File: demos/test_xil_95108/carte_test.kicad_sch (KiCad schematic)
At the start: 44 parts

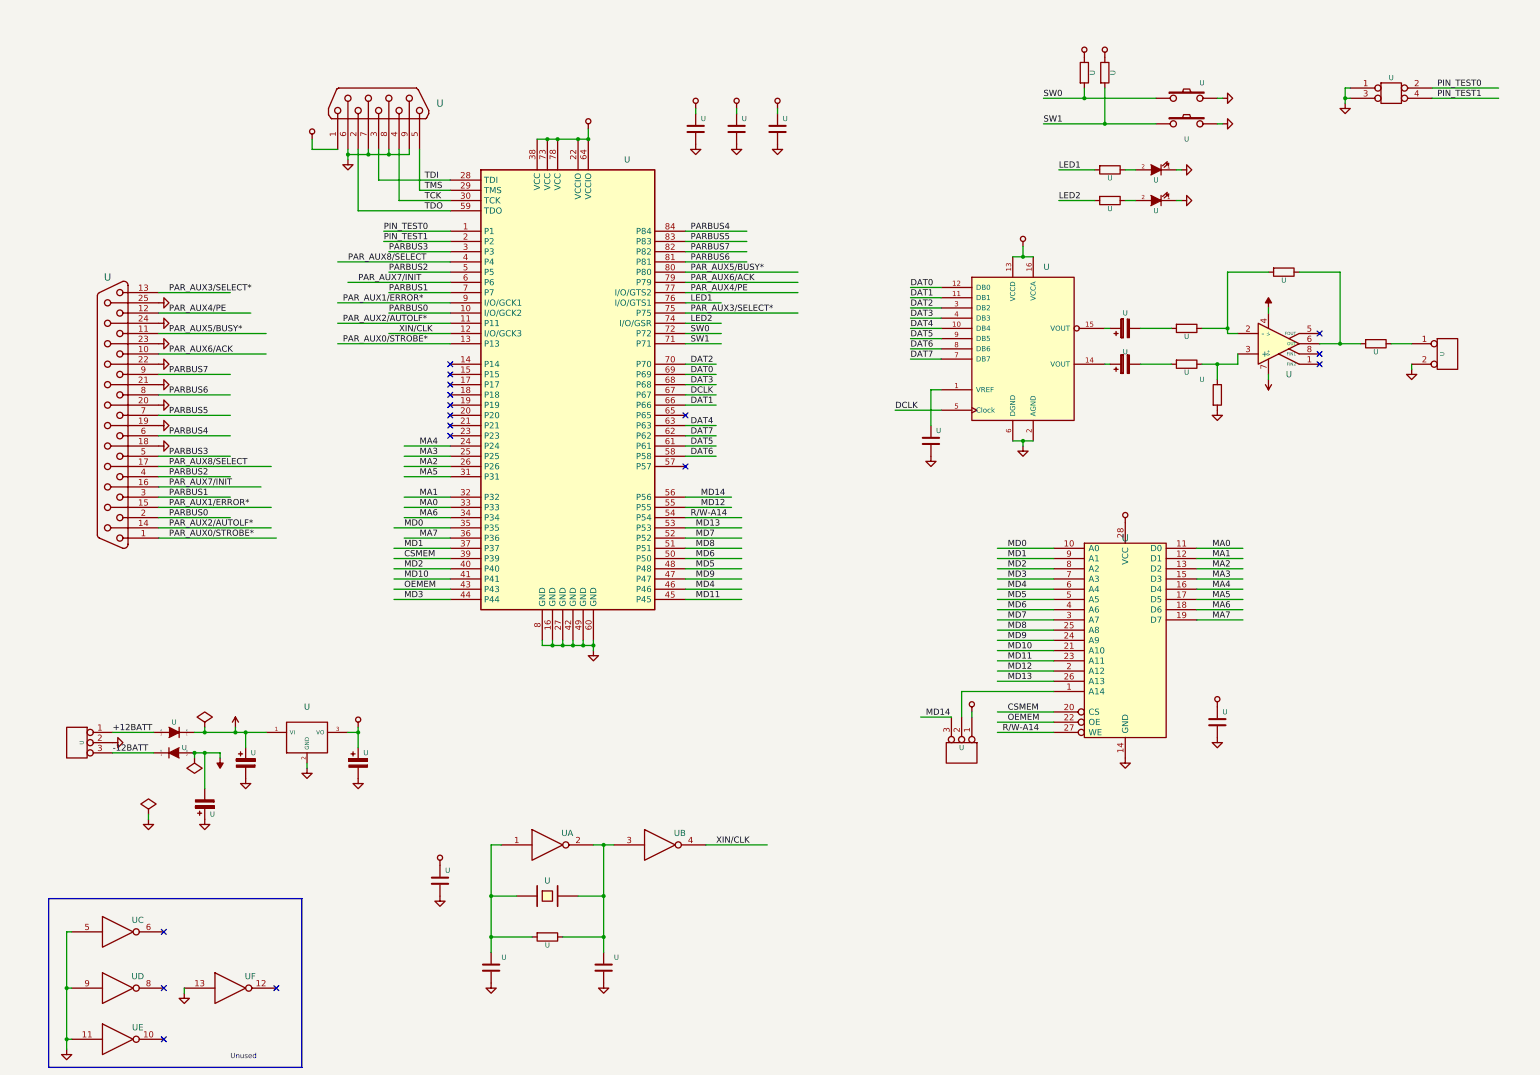
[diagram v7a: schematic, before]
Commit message: Update demos using latest file formats.
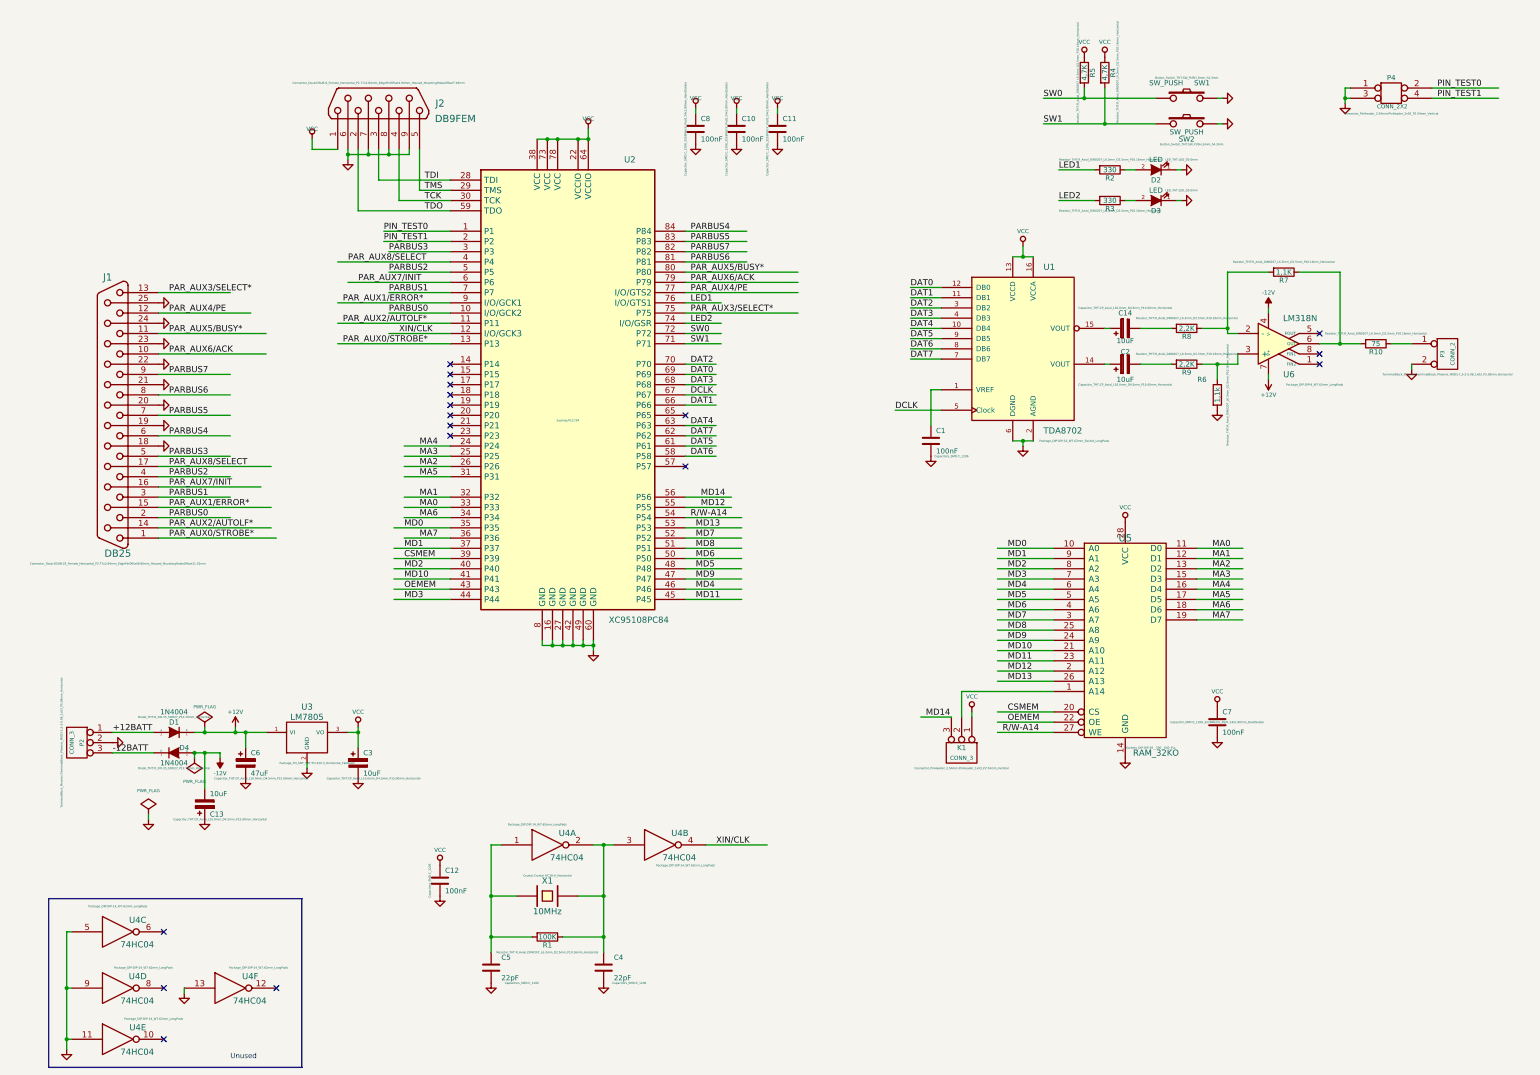
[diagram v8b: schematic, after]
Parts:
- removed U (x2): (no value), symbol carte_test_schlib:-12V
- C1, C12: renamed from U; value (none) -> 100nF; footprint (none) -> Capacitors_SMD:C_1206
- C10, C11, C7, C8: renamed from U; value (none) -> 100nF; footprint (none) -> Capacitor_SMD:C_1206_3216Metric_Pad1.24x1.80mm_HandSolder
- C13, C14, C2, C3: renamed from U; value (none) -> 10uF; footprint (none) -> Capacitor_THT:CP_Axial_L10.0mm_D4.5mm_P15.00mm_Horizontal
- C4, C5: renamed from U; value (none) -> 22pF; footprint (none) -> Capacitors_SMD:C_1206
- C6: renamed from U; value (none) -> 47uF; footprint (none) -> Capacitor_THT:CP_Axial_L10.0mm_D4.5mm_P15.00mm_Horizontal
- D1, D4: renamed from U; value (none) -> 1N4004; footprint (none) -> Diode_THT:D_DO-35_SOD27_P12.70mm_Horizontal
- D2, D3: renamed from U; value (none) -> LED; footprint (none) -> LED_THT:LED_D5.0mm
- J1: renamed from U; value (none) -> DB25; footprint (none) -> Connector_Dsub:DSUB-25_Female_Horizontal_P2.77x2.84mm_EdgePinOffset9.90mm_Housed_MountingHolesOffset11.32mm
- J2: renamed from U; value (none) -> DB9FEM; footprint (none) -> Connector_Dsub:DSUB-9_Female_Horizontal_P2.77x2.84mm_EdgePinOffset4.94mm_Housed_MountingHolesOffset7.48mm
- K1: renamed from U; value (none) -> CONN_3; footprint (none) -> Connector_PinHeader_2.54mm:PinHeader_1x03_P2.54mm_Vertical
- P2: renamed from U; value (none) -> CONN_3; footprint (none) -> TerminalBlock_Phoenix:TerminalBlock_Phoenix_MKDS-1,5-3-5.08_1x03_P5.08mm_Horizontal
- P3: renamed from U; value (none) -> CONN_2; footprint (none) -> TerminalBlock_Phoenix:TerminalBlock_Phoenix_MKDS-1,5-2-5.08_1x02_P5.08mm_Horizontal
- P4: renamed from U; value (none) -> CONN_2X2; footprint (none) -> Connector_PinHeader_2.54mm:PinHeader_2x02_P2.54mm_Vertical
- R1: renamed from U; value (none) -> 100K; footprint (none) -> Resistor_THT:R_Axial_DIN0207_L6.3mm_D2.5mm_P10.16mm_Horizontal
- R10: renamed from U; value (none) -> 75; footprint (none) -> Resistor_THT:R_Axial_DIN0207_L6.3mm_D2.5mm_P10.16mm_Horizontal
- R2, R3: renamed from U; value (none) -> 330; footprint (none) -> Resistor_THT:R_Axial_DIN0207_L6.3mm_D2.5mm_P10.16mm_Horizontal
- R4, R5: renamed from U; value (none) -> 4,7K; footprint (none) -> Resistor_THT:R_Axial_DIN0207_L6.3mm_D2.5mm_P10.16mm_Horizontal
- R6: renamed from U; value (none) -> 1,1k; footprint (none) -> Resistor_THT:R_Axial_DIN0207_L6.3mm_D2.5mm_P10.16mm_Horizontal
- R7: renamed from U; value (none) -> 1,1K; footprint (none) -> Resistor_THT:R_Axial_DIN0207_L6.3mm_D2.5mm_P10.16mm_Horizontal
- R8, R9: renamed from U; value (none) -> 2,2K; footprint (none) -> Resistor_THT:R_Axial_DIN0207_L6.3mm_D2.5mm_P10.16mm_Horizontal
- SW1, SW2: renamed from U; value (none) -> SW_PUSH; footprint (none) -> Button_Switch_THT:SW_PUSH_6mm_h4.3mm
- U1: renamed from U; value (none) -> TDA8702; footprint (none) -> Package_DIP:DIP-16_W7.62mm_Socket_LongPads
- U2: renamed from U; value (none) -> XC95108PC84; footprint (none) -> Sockets:PLCC84
- U3: renamed from U; value (none) -> LM7805; footprint (none) -> Package_TO_SOT_THT:TO-220-3_Horizontal_TabDown
- U4: renamed from U; value (none) -> 74HC04; footprint (none) -> Package_DIP:DIP-14_W7.62mm_LongPads
- U5: renamed from U; value (none) -> RAM_32KO; footprint (none) -> Sockets_DIP:DIP-28__300__600_ELL
- U6: renamed from U; value (none) -> LM318N; footprint (none) -> Package_DIP:DIP-8_W7.62mm_LongPads
- X1: renamed from U; value (none) -> 10MHz; footprint (none) -> Crystal:Crystal_HC18-U_Horizontal
